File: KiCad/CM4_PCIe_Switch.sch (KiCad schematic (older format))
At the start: 17 parts, among them IC2 PI7C9X2G404SLBFDE, U4 AP7363-10D

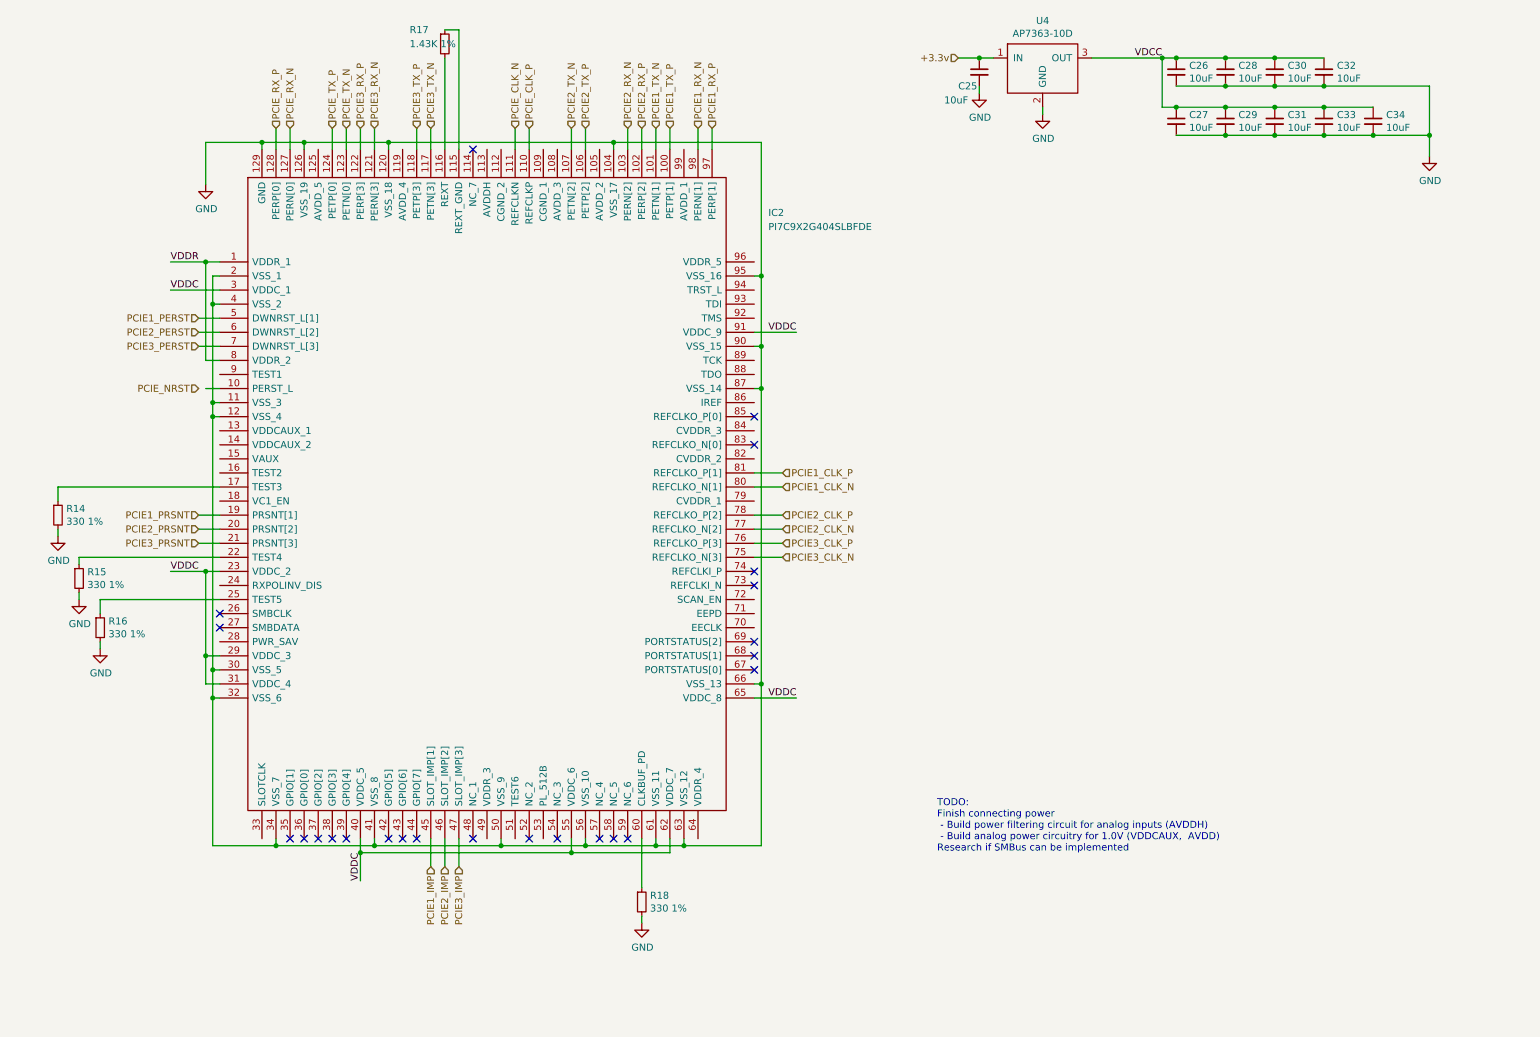
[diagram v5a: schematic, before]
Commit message: Updated PCI-e switch with more power wiring
Still needs more work on connectivity before #28 can be solved.
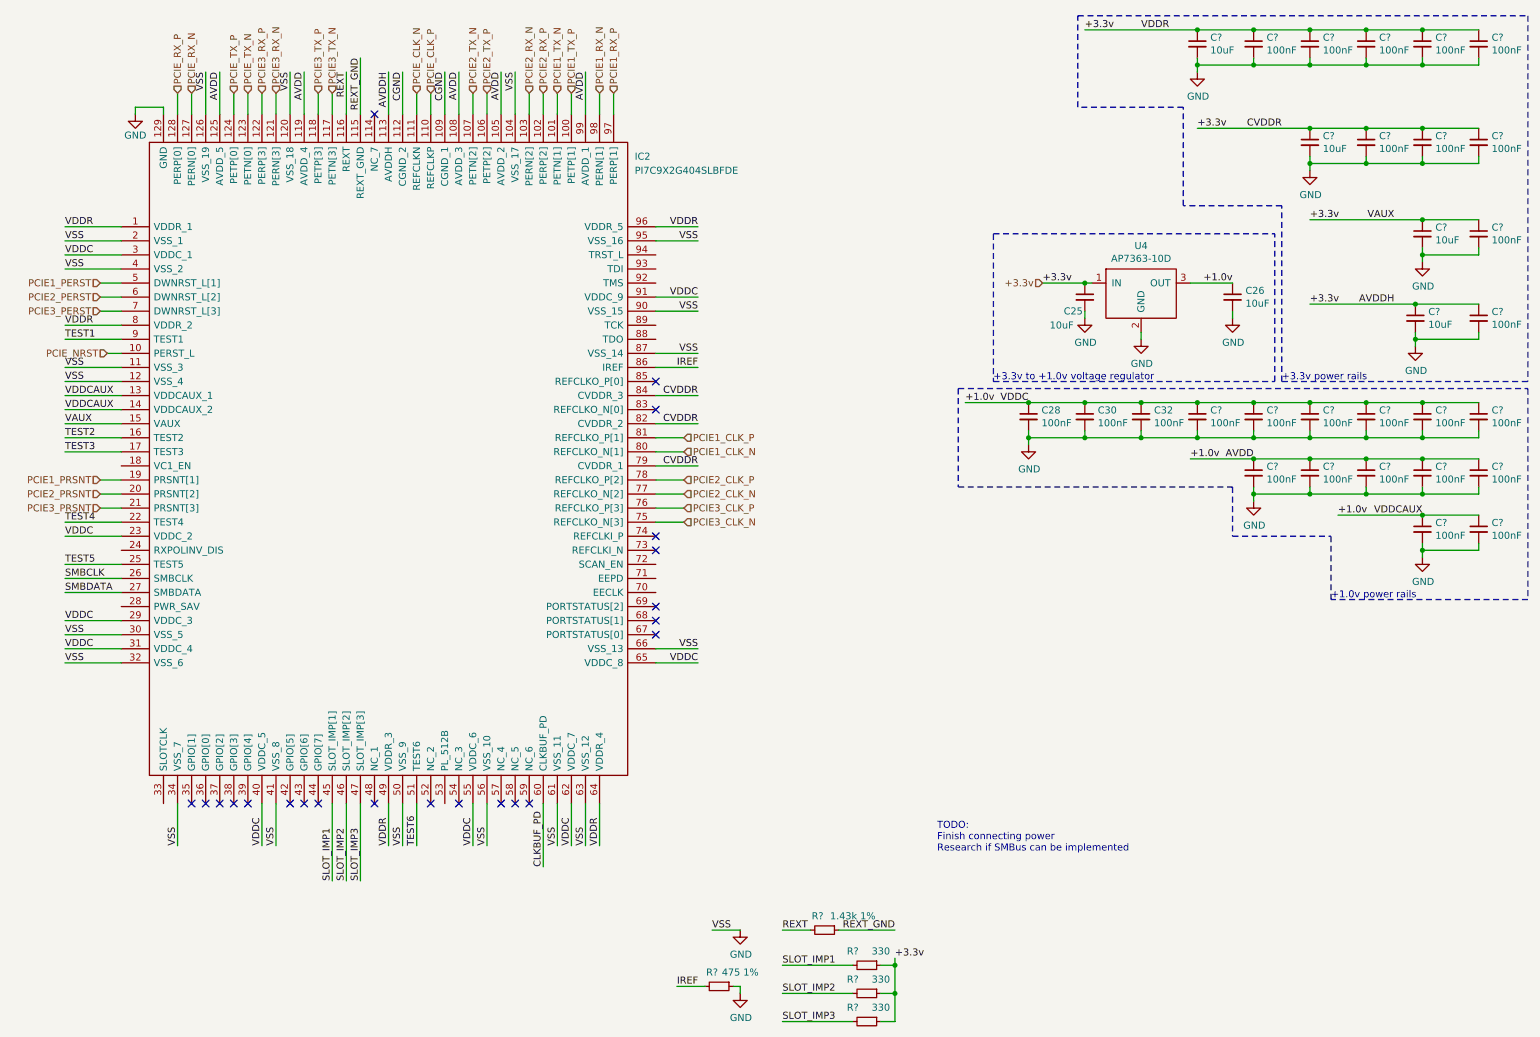
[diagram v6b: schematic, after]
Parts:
- removed C27, C29, C31, C33, C34: 10uF, symbol Device:C_Small
- removed R14, R15, R16, R18: 330 1%, symbol Device:R_Small
- removed R17: 1.43K 1%, symbol Device:R_Small
- added C? (x23): 100nF, symbol Device:C_Small
- added C? (x4): 10uF, symbol Device:C_Small
- added R? (x3): 330, symbol Device:R_Small
- added R?: 475 1%, symbol Device:R_Small
- added R?: 1.43k 1%, symbol Device:R_Small
- C28, C30, C32: value 10uF -> 100nF
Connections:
- net VDCC is gone; now on net +1.0v: C26.1, C28.1, C30.1, C32.1, U4.3 (OUT)
- net VDDC is gone; now on net +1.0v: IC2.23 (VDDC_2), IC2.29 (VDDC_3), IC2.3 (VDDC_1), IC2.31 (VDDC_4), IC2.40 (VDDC_5), IC2.55 (VDDC_6), IC2.62 (VDDC_7), IC2.65 (VDDC_8), IC2.91 (VDDC_9)
- net VDDR is gone; now on net +3.3v: IC2.1 (VDDR_1), IC2.8 (VDDR_2)
- net +3.3v: now also IC2.113 (AVDDH), IC2.15 (VAUX), IC2.49 (VDDR_3), IC2.64 (VDDR_4), IC2.79 (CVDDR_1), IC2.82 (CVDDR_2), IC2.84 (CVDDR_3), IC2.96 (VDDR_5), C?.1, C?.1, C?.1, C?.1, C?.1, C?.1, C?.1, C?.1, C?.1, C?.1, C?.1, C?.1, C?.1, C?.1, R?.1, R?.1, R?.1
- net GND: now also C?.2, C?.2, C?.2, C?.2, C?.2, C?.2, C?.2, C?.2, C?.2, C?.2, C?.2, C?.2, C?.2, C?.2, C?.2, C?.2, C?.2, C?.2, C?.2, C?.2, C?.2, C?.2, C?.2, C?.2, C?.2, C?.2, C?.2, R?.1
- net PCIE_NRST: now also IC2.10 (PERST_L)
- net TEST3: now reaches IC2.17 (TEST3)
- net TEST4: now reaches IC2.22 (TEST4)
- net TEST5: now reaches IC2.25 (TEST5)
- net CLKBUF_PD: now reaches IC2.60 (CLKBUF_PD)
- net REXT_GND: now reaches IC2.115 (REXT_GND)
- net REXT_GND: now also R?.1
- net REXT: now reaches IC2.116 (REXT)
- net REXT: now also R?.2
- net +1.0v: now reaches IC2.105 (AVDD_2)
- net +1.0v: now also IC2.108 (AVDD_3), IC2.119 (AVDD_4), IC2.125 (AVDD_5), IC2.13 (VDDCAUX_1), IC2.14 (VDDCAUX_2), IC2.99 (AVDD_1), C?.1, C?.1, C?.1, C?.1, C?.1, C?.1, C?.1, C?.1, C?.1, C?.1, C?.1, C?.1, C?.1
- net CGND: now reaches IC2.109 (CGND_1)
- net CGND: now also IC2.112 (CGND_2)
- net TEST2: now reaches IC2.16 (TEST2)
- net SMBCLK: now reaches IC2.26 (SMBCLK)
- net SMBDATA: now reaches IC2.27 (SMBDATA)
- net TEST6: now reaches IC2.51 (TEST6)
- net IREF: now reaches IC2.86 (IREF)
- net IREF: now also R?.2
- net TEST1: now reaches IC2.9 (TEST1)
- net PCIE1_IMP renamed SLOT_IMP1
- net SLOT_IMP1: now also R?.2
- net PCIE2_IMP renamed SLOT_IMP2
- net SLOT_IMP2: now also R?.2
- net PCIE3_IMP renamed SLOT_IMP3
- net SLOT_IMP3: now also R?.2
- no-connect marks 24 -> 22
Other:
- note added: "+1.0v power rails"
- note added: "+3.3v power rails"
- note added: "+3.3v to +1.0v voltage regulator"
- note added: "TODO:\nFinish connecting power\nResearch if SMBus can be implemented"
- note removed: "TODO:\nFinish connecting power\n - Build power filtering circuit for analog inputs (AVDDH)\n - Build analog power circuitry for 1.0V (VDDCAUX, AVDD)\nResearch if SMBus can be implemented"
- moved on the sheet: C25, C26, C28, C30, C32, IC2, U4
